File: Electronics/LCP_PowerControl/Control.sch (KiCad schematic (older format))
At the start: 2 parts, among them J2 Conn_01x05_Shielded

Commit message: Adding libraries and recent changes
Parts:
- added J?: Conn_02x04_Odd_Even, Connector_PinSocket_2.54mm:PinSocket_2x04_P2.54mm_Vertical, symbol Connector_Generic:Conn_02x04_Odd_Even
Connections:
- net CONTROL_EN: now also J?.1 (Pin_1)
- net CONTROL_SCL: now also J?.3 (Pin_3)
- net CONTROL_SDA: now also J?.5 (Pin_5)
- net GND: now also J?.2 (Pin_2), J?.4 (Pin_4), J?.6 (Pin_6), J?.8 (Pin_8)
- no-connect marks 0 -> 1
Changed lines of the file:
@@
 $Descr A4 11693 8268
 encoding utf-8
-Sheet 6 8
+Sheet 5 11
 Title ""
 Date ""
@@
 CONTROL_SCL
 Wire Wire Line
-	8950 3700 4400 3700
+	8950 3800 7300 3800
 Wire Wire Line
-	8950 3800 4400 3800
-Wire Wire Line
-	4400 3900 8950 3900
+	4400 3900 7200 3900
 $Comp
 L power:GND #PWR010
@@
 Wire Wire Line
 	4400 3600 4800 3600
+$Comp
+L power:GND #PWR?
+U 1 1 5EED44A2
+P 7100 5200
+F 0 "#PWR?" H 7100 4950 50  0001 C CNN
+F 1 "GND" H 7105 5027 50  0000 C CNN
+F 2 "" H 7100 5200 50  0001 C CNN
+F 3 "" H 7100 5200 50  0001 C CNN
+	1    7100 5200
+	1    0    0    -1
+$EndComp
+Wire Wire Line
+	7100 5200 7100 5050
+Wire Wire Line
+	7200 5000 7200 5050
+Wire Wire Line
+	7200 5050 7100 5050
+Connection ~ 7100 5050
+Wire Wire Line
+	7100 5050 7100 5000
+Wire Wire Line
+	7300 5000 7300 5050
+Connection ~ 7200 5050
+$Comp
+L Connector_Generic:Conn_02x04_Odd_Even J?
+U 1 1 5EED0364
+P 7200 4700
+F 0 "J?" V 7159 4412 50  0000 R CNN
+F 1 "Conn_02x04_Odd_Even" V 7250 4412 50  0000 R CNN
+F 2 "Connector_PinSocket_2.54mm:PinSocket_2x04_P2.54mm_Vertical" H 7200 4700 50  0001 C CNN
+F 3 "~" H 7200 4700 50  0001 C CNN
+F 4 "SALEAE_TEST" V 7341 4412 50  0000 R CNN "Field4"
+	1    7200 4700
+	0    -1   1    0
+$EndComp
+Wire Wire Line
+	7400 5000 7400 5050
+Wire Wire Line
+	7200 5050 7300 5050
+Wire Wire Line
+	7300 5050 7400 5050
+Connection ~ 7300 5050
+Wire Wire Line
+	7100 4500 7100 3700
+Wire Wire Line
+	4400 3700 7100 3700
+Connection ~ 7100 3700
+Wire Wire Line
+	7100 3700 8950 3700
+Wire Wire Line
+	7200 4500 7200 3900
+Connection ~ 7200 3900
+Wire Wire Line
+	7200 3900 8950 3900
+Wire Wire Line
+	7300 4500 7300 3800
+Connection ~ 7300 3800
+Wire Wire Line
+	7300 3800 4400 3800
+NoConn ~ 7400 4500
 $EndSCHEMATC

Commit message: Aiming for rev 0.1 complete
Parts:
- removed J2: Conn_01x05_Shielded, symbol Connector_Generic_Shielded:Conn_01x05_Shielded
- added J2: Conn_01x05, Connector_PinHeader_2.54mm:PinHeader_1x05_P2.54mm_Vertical, symbol Connector_Generic:Conn_01x05
- gave numbers to parts that had none: 1
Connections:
- net CONTROL_EN: now also J2.4 (Pin_4)
- net CONTROL_SCL: now also J2.2 (Pin_2)
- net CONTROL_SDA: now also J2.3 (Pin_3)
- net GND: now also J2.1 (Pin_1)
- net at F1.2: now also J2.5 (Pin_5)
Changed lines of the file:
@@
 Sheet 5 11
 Title ""
-Date ""
-Rev ""
+Date "2020-06-17"
+Rev "R0.1"
 Comp ""
-Comment1 ""
+Comment1 "Design by: Matt Casari"
 Comment2 ""
 Comment3 ""
@@
 Text HLabel 8950 3800 2    50   BiDi ~ 0
 CONTROL_SDA
-$Comp
-L Connector_Generic_Shielded:Conn_01x05_Shielded J2
-U 1 1 5EE2F074
-P 4200 3800
-F 0 "J2" H 4288 3671 50  0000 L CNN
-F 1 "Conn_01x05_Shielded" H 4288 3762 50  0000 L CNN
-F 2 "" H 4200 3800 50  0001 C CNN
-F 3 "~" H 4200 3800 50  0001 C CNN
-	1    4200 3800
-	-1   0    0    1
-$EndComp
 Text HLabel 8950 3700 2    50   Output ~ 0
 CONTROL_EN
@@
 	4400 3600 4800 3600
 $Comp
-L power:GND #PWR?
+L power:GND #PWR034
 U 1 1 5EED44A2
 P 7100 5200
-F 0 "#PWR?" H 7100 4950 50  0001 C CNN
+F 0 "#PWR034" H 7100 4950 50  0001 C CNN
 F 1 "GND" H 7105 5027 50  0000 C CNN
 F 2 "" H 7100 5200 50  0001 C CNN
@@
 Connection ~ 7200 5050
 $Comp
-L Connector_Generic:Conn_02x04_Odd_Even J?
+L Connector_Generic:Conn_02x04_Odd_Even J15
 U 1 1 5EED0364
 P 7200 4700
-F 0 "J?" V 7159 4412 50  0000 R CNN
+F 0 "J15" V 7159 4412 50  0000 R CNN
 F 1 "Conn_02x04_Odd_Even" V 7250 4412 50  0000 R CNN
 F 2 "Connector_PinSocket_2.54mm:PinSocket_2x04_P2.54mm_Vertical" H 7200 4700 50  0001 C CNN
@@
 	7300 3800 4400 3800
 NoConn ~ 7400 4500
+$Comp
+L Connector_Generic:Conn_01x05 J2
+U 1 1 5EED17CB
+P 4200 3800
+F 0 "J2" H 4118 3375 50  0000 C CNN
+F 1 "Conn_01x05" H 4118 3466 50  0000 C CNN
+F 2 "Connector_PinHeader_2.54mm:PinHeader_1x05_P2.54mm_Vertical" H 4200 3800 50  0001 C CNN
+F 3 "~" H 4200 3800 50  0001 C CNN
+	1    4200 3800
+	-1   0    0    1
+$EndComp
 $EndSCHEMATC

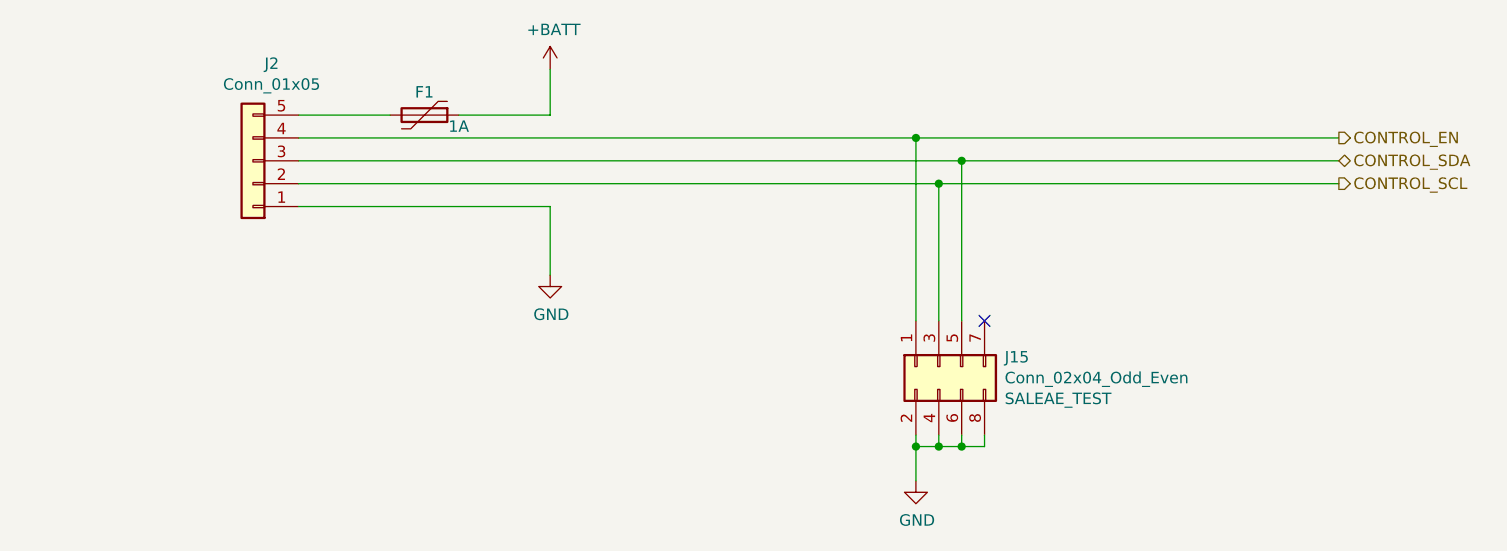
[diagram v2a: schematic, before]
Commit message: Rev1
Removed test points. Cleaned up unnecessary traces. Fixed electrical issues #1-#7
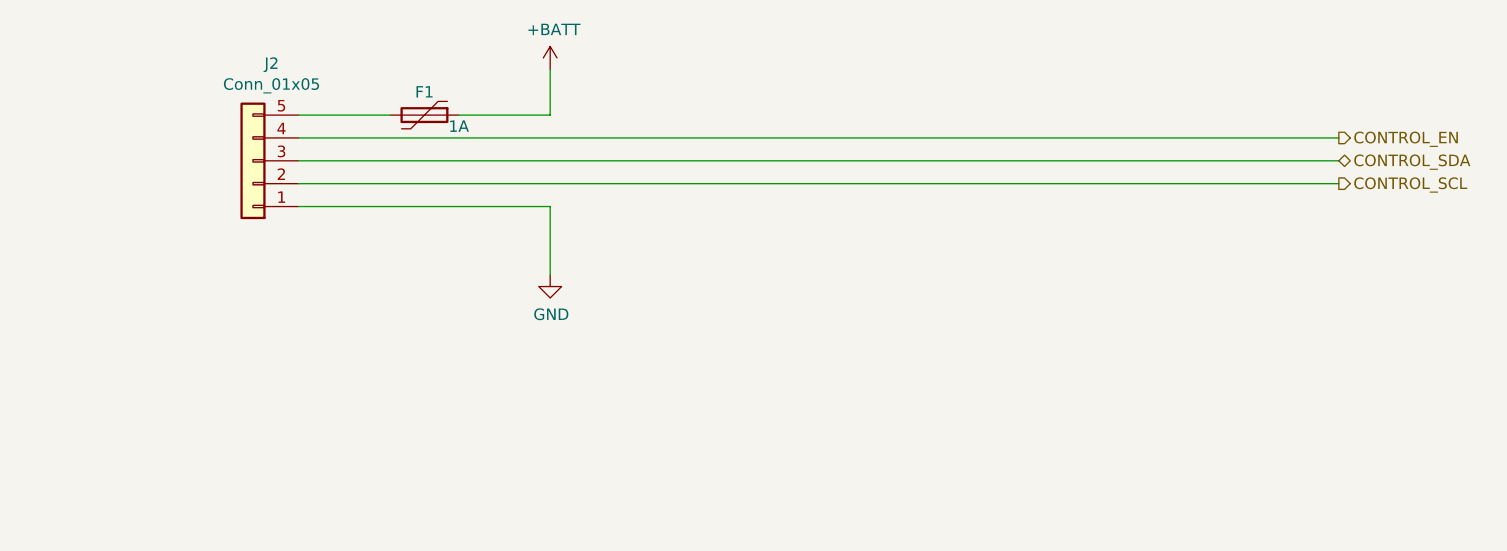
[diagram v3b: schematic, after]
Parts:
- removed J15: Conn_02x04_Odd_Even, Connector_PinSocket_2.54mm:PinSocket_2x04_P2.54mm_Vertical, symbol Connector_Generic:Conn_02x04_Odd_Even
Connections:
- no-connect marks 1 -> 0
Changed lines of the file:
@@
 Text HLabel 8950 3900 2    50   Output ~ 0
 CONTROL_SCL
-Wire Wire Line
-	8950 3800 7300 3800
-Wire Wire Line
-	4400 3900 7200 3900
 $Comp
 L power:GND #PWR010
@@
 	4400 3600 4800 3600
 $Comp
-L power:GND #PWR034
-U 1 1 5EED44A2
-P 7100 5200
-F 0 "#PWR034" H 7100 4950 50  0001 C CNN
-F 1 "GND" H 7105 5027 50  0000 C CNN
-F 2 "" H 7100 5200 50  0001 C CNN
-F 3 "" H 7100 5200 50  0001 C CNN
-	1    7100 5200
-	1    0    0    -1
-$EndComp
-Wire Wire Line
-	7100 5200 7100 5050
-Wire Wire Line
-	7200 5000 7200 5050
-Wire Wire Line
-	7200 5050 7100 5050
-Connection ~ 7100 5050
-Wire Wire Line
-	7100 5050 7100 5000
-Wire Wire Line
-	7300 5000 7300 5050
-Connection ~ 7200 5050
-$Comp
-L Connector_Generic:Conn_02x04_Odd_Even J15
-U 1 1 5EED0364
-P 7200 4700
-F 0 "J15" V 7159 4412 50  0000 R CNN
-F 1 "Conn_02x04_Odd_Even" V 7250 4412 50  0000 R CNN
-F 2 "Connector_PinSocket_2.54mm:PinSocket_2x04_P2.54mm_Vertical" H 7200 4700 50  0001 C CNN
-F 3 "~" H 7200 4700 50  0001 C CNN
-F 4 "SALEAE_TEST" V 7341 4412 50  0000 R CNN "Field4"
-	1    7200 4700
-	0    -1   1    0
-$EndComp
-Wire Wire Line
-	7400 5000 7400 5050
-Wire Wire Line
-	7200 5050 7300 5050
-Wire Wire Line
-	7300 5050 7400 5050
-Connection ~ 7300 5050
-Wire Wire Line
-	7100 4500 7100 3700
-Wire Wire Line
-	4400 3700 7100 3700
-Connection ~ 7100 3700
-Wire Wire Line
-	7100 3700 8950 3700
-Wire Wire Line
-	7200 4500 7200 3900
-Connection ~ 7200 3900
-Wire Wire Line
-	7200 3900 8950 3900
-Wire Wire Line
-	7300 4500 7300 3800
-Connection ~ 7300 3800
-Wire Wire Line
-	7300 3800 4400 3800
-NoConn ~ 7400 4500
-$Comp
 L Connector_Generic:Conn_01x05 J2
 U 1 1 5EED17CB
@@
 	-1   0    0    1
 $EndComp
+Wire Wire Line
+	4400 3800 8950 3800
+Wire Wire Line
+	4400 3900 8950 3900
+Wire Wire Line
+	4400 3700 8950 3700
 $EndSCHEMATC

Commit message: BOM Update
Updated MPNs on components to match supplies as well as correcting some resistor values
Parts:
- F1: MPN MF-R065 -> MF-R090
- J2: MPN (none) -> 61300511121
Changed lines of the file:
@@
 F 2 "Fuse:Fuse_Bourns_MF-RG650" H 5000 3400 50  0001 L CNN
 F 3 "~" H 4950 3600 50  0001 C CNN
-F 4 "MF-R065" V 4950 3600 50  0001 C CNN "MPN"
+F 4 "MF-R090" V 4950 3600 50  0001 C CNN "MPN"
 	1    4950 3600
 	0    1    1    0
@@
 F 2 "Connector_PinHeader_2.54mm:PinHeader_1x05_P2.54mm_Vertical" H 4200 3800 50  0001 C CNN
 F 3 "~" H 4200 3800 50  0001 C CNN
+F 4 "61300511121" H 4200 3800 50  0001 C CNN "MPN"
 	1    4200 3800
 	-1   0    0    1
